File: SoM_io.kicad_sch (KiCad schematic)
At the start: 1 part, among them J2 Hermaphroditic_Molex_203456-0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

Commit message: [#81970] Refactor root
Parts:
- renumbered J2 to J1
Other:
- moved on the sheet: J1C, J1G, J1H, J1I, J1K

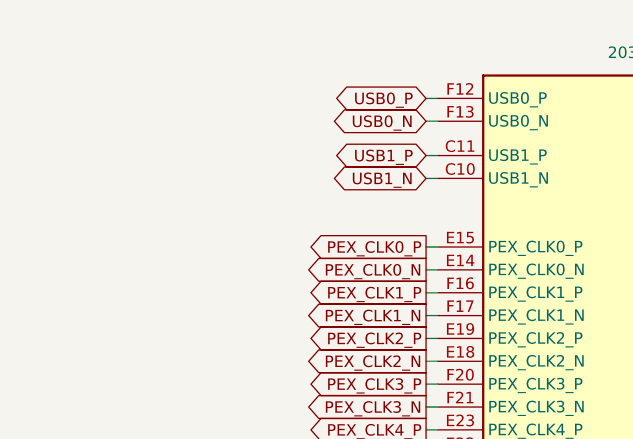
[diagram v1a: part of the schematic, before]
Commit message: [#82048] Add bus definitions and bus connections from M.2 key M to SoM
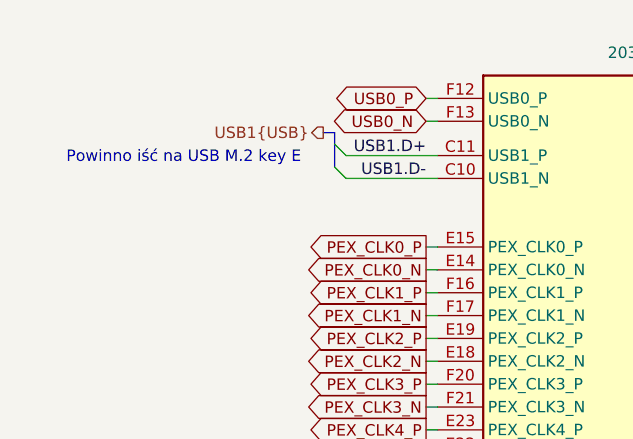
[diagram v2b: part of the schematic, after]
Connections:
- net USB1_N renamed USB1.D-
- net USB1_P renamed USB1.D+
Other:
- note added: "Powinno iść na USB M.2 key E"
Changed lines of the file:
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@@
 		(comment 1 "www.antmicro.com")
 	)
+	(text "Powinno iść na USB M.2 key E"
+		(exclude_from_sim no)
+		(at 89.916 68.834 0)
+		(effects
+			(font
+				(size 1.27 1.27)
+			)
+		)
+	)
+	(bus_entry
+		(at 107.95 68.58)
+		(size -1.27 -1.27)
+		(stroke
+			(width 0)
+			(type default)
+		)
+	)
+	(bus_entry
+		(at 107.95 71.12)
+		(size -1.27 -1.27)
+		(stroke
+			(width 0)
+			(type default)
+		)
+	)
 	(wire
 		(pts
@@
 		)
 	)
+	(bus
+		(pts
+			(xy 106.68 67.31) (xy 106.68 66.04)
+		)
+		(stroke
+			(width 0)
+			(type default)
+		)
+	)
 	(wire
 		(pts
@@
 	(wire
 		(pts
+			(xy 107.95 71.12) (xy 118.11 71.12)
+		)
+		(stroke
+			(width 0)
+			(type default)
+		)
+	)
+	(wire
+		(pts
 			(xy 166.37 165.1) (xy 163.83 165.1)
 		)
@@
 		)
 	)
+	(bus
+		(pts
+			(xy 106.68 66.04) (xy 105.41 66.04)
+		)
+		(stroke
+			(width 0)
+			(type default)
+		)
+	)
 	(wire
 		(pts
@@
 	(wire
 		(pts
-			(xy 116.84 71.12) (xy 118.11 71.12)
+			(xy 107.95 68.58) (xy 118.11 68.58)
 		)
 		(stroke
@@
 	(wire
 		(pts
-			(xy 116.84 68.58) (xy 118.11 68.58)
-		)
-		(stroke
-			(width 0)
-			(type default)
-		)
-	)
-	(wire
-		(pts
 			(xy 222.25 85.09) (xy 223.52 85.09)
 		)
@@
 		)
 	)
+	(bus
+		(pts
+			(xy 106.68 69.85) (xy 106.68 67.31)
+		)
+		(stroke
+			(width 0)
+			(type default)
+		)
+	)
 	(wire
 		(pts
@@
 		)
 	)
+	(label "USB1.D+"
+		(at 116.84 68.58 180)
+		(effects
+			(font
+				(size 1.27 1.27)
+			)
+			(justify right bottom)
+		)
+	)
+	(label "USB1.D-"
+		(at 116.84 71.12 180)
+		(effects
+			(font
+				(size 1.27 1.27)
+			)
+			(justify right bottom)
+		)
+	)
 	(global_label "GPIO08/DMIC3_5_DAT"
 		(shape input)
@@
 		)
 	)
-	(global_label "USB1_P"
-		(shape bidirectional)
-		(at 116.84 68.58 180)
-		(effects
-			(font
-				(size 1.27 1.27)
-			)
-			(justify right)
-		)
-		(property "Intersheetrefs" "${INTERSHEET_REFS}"
-			(at 116.84 68.58 0)
-			(effects
-				(font
-					(size 1.27 1.27)
-				)
-				(hide yes)
-			)
-		)
-	)
 	(global_label "PEX_C1_RST_N"
 		(shape output)
@@
 		)
 	)
-	(global_label "USB1_N"
-		(shape bidirectional)
-		(at 116.84 71.12 180)
-		(effects
-			(font
-				(size 1.27 1.27)
-			)
-			(justify right)
-		)
-		(property "Intersheetrefs" "${INTERSHEET_REFS}"
-			(at 116.84 71.12 0)
-			(effects
-				(font
-					(size 1.27 1.27)
-				)
-				(hide yes)
-			)
-		)
-	)
 	(global_label "UART1_TX"
 		(shape output)
@@
 		)
 	)
+	(hierarchical_label "USB1{USB}"
+		(shape output)
+		(at 105.41 66.04 180)
+		(effects
+			(font
+				(size 1.27 1.27)
+			)
+			(justify right)
+		)
+	)

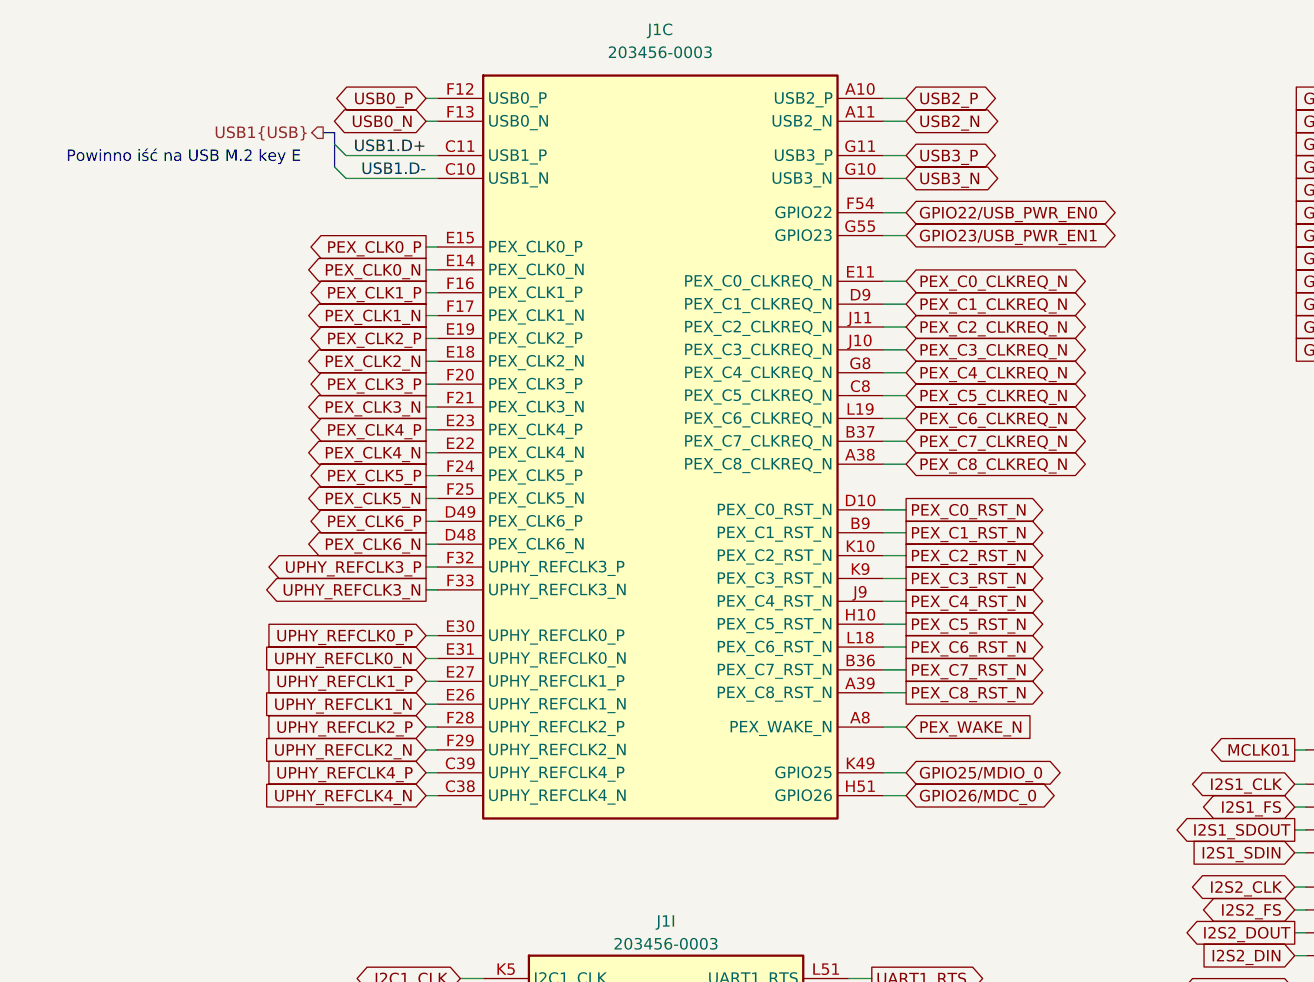
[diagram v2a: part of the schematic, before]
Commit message: [#82048] Continue routing bus connections from M.2 key M to SoM
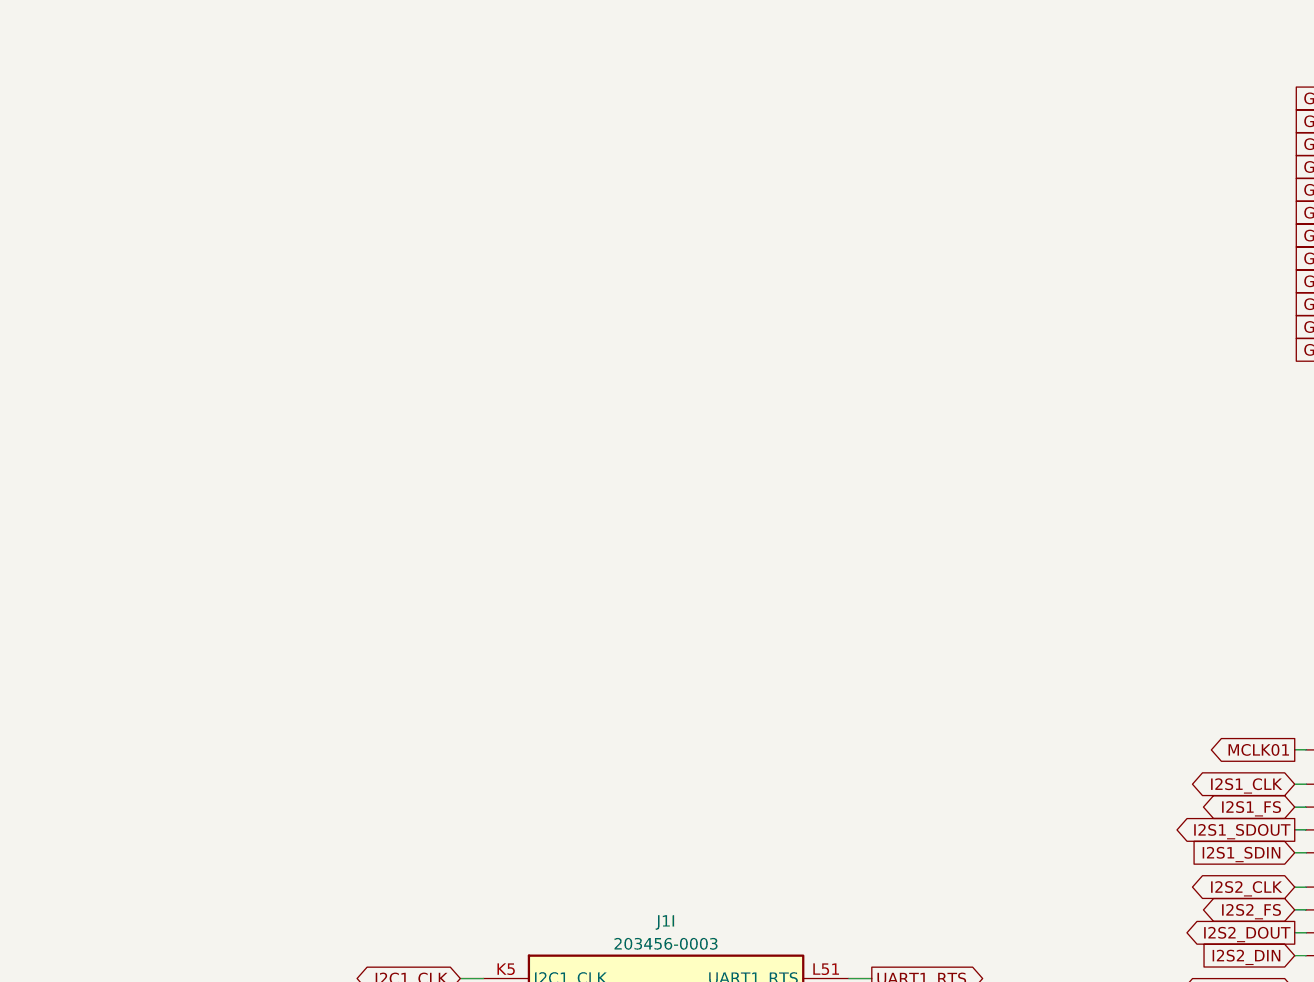
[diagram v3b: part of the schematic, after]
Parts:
- removed unit 3 of J1
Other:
- note removed: "Powinno iść na USB M.2 key E"

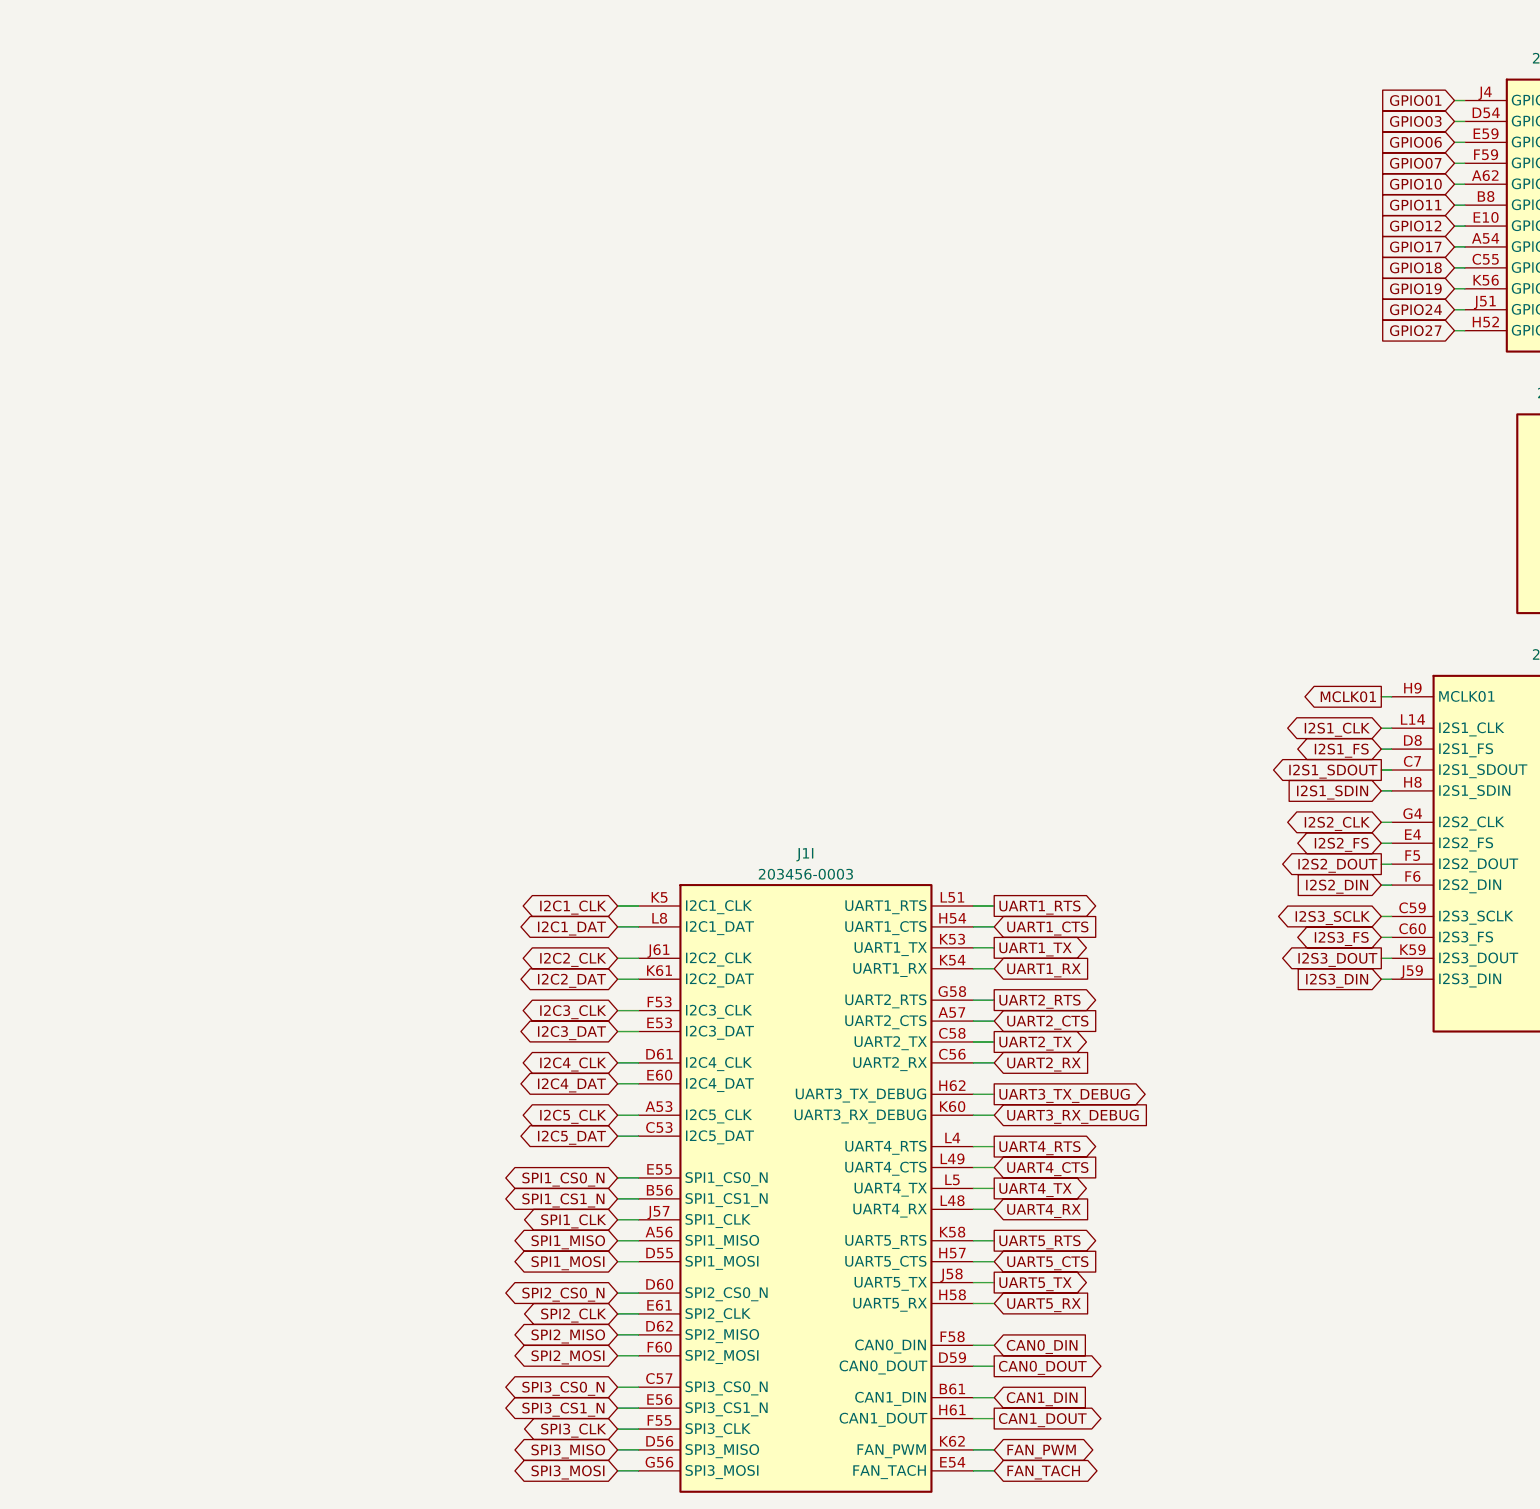
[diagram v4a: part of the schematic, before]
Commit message: [#82048] Route UART, I2S and I2C from M.2 key E to SoM
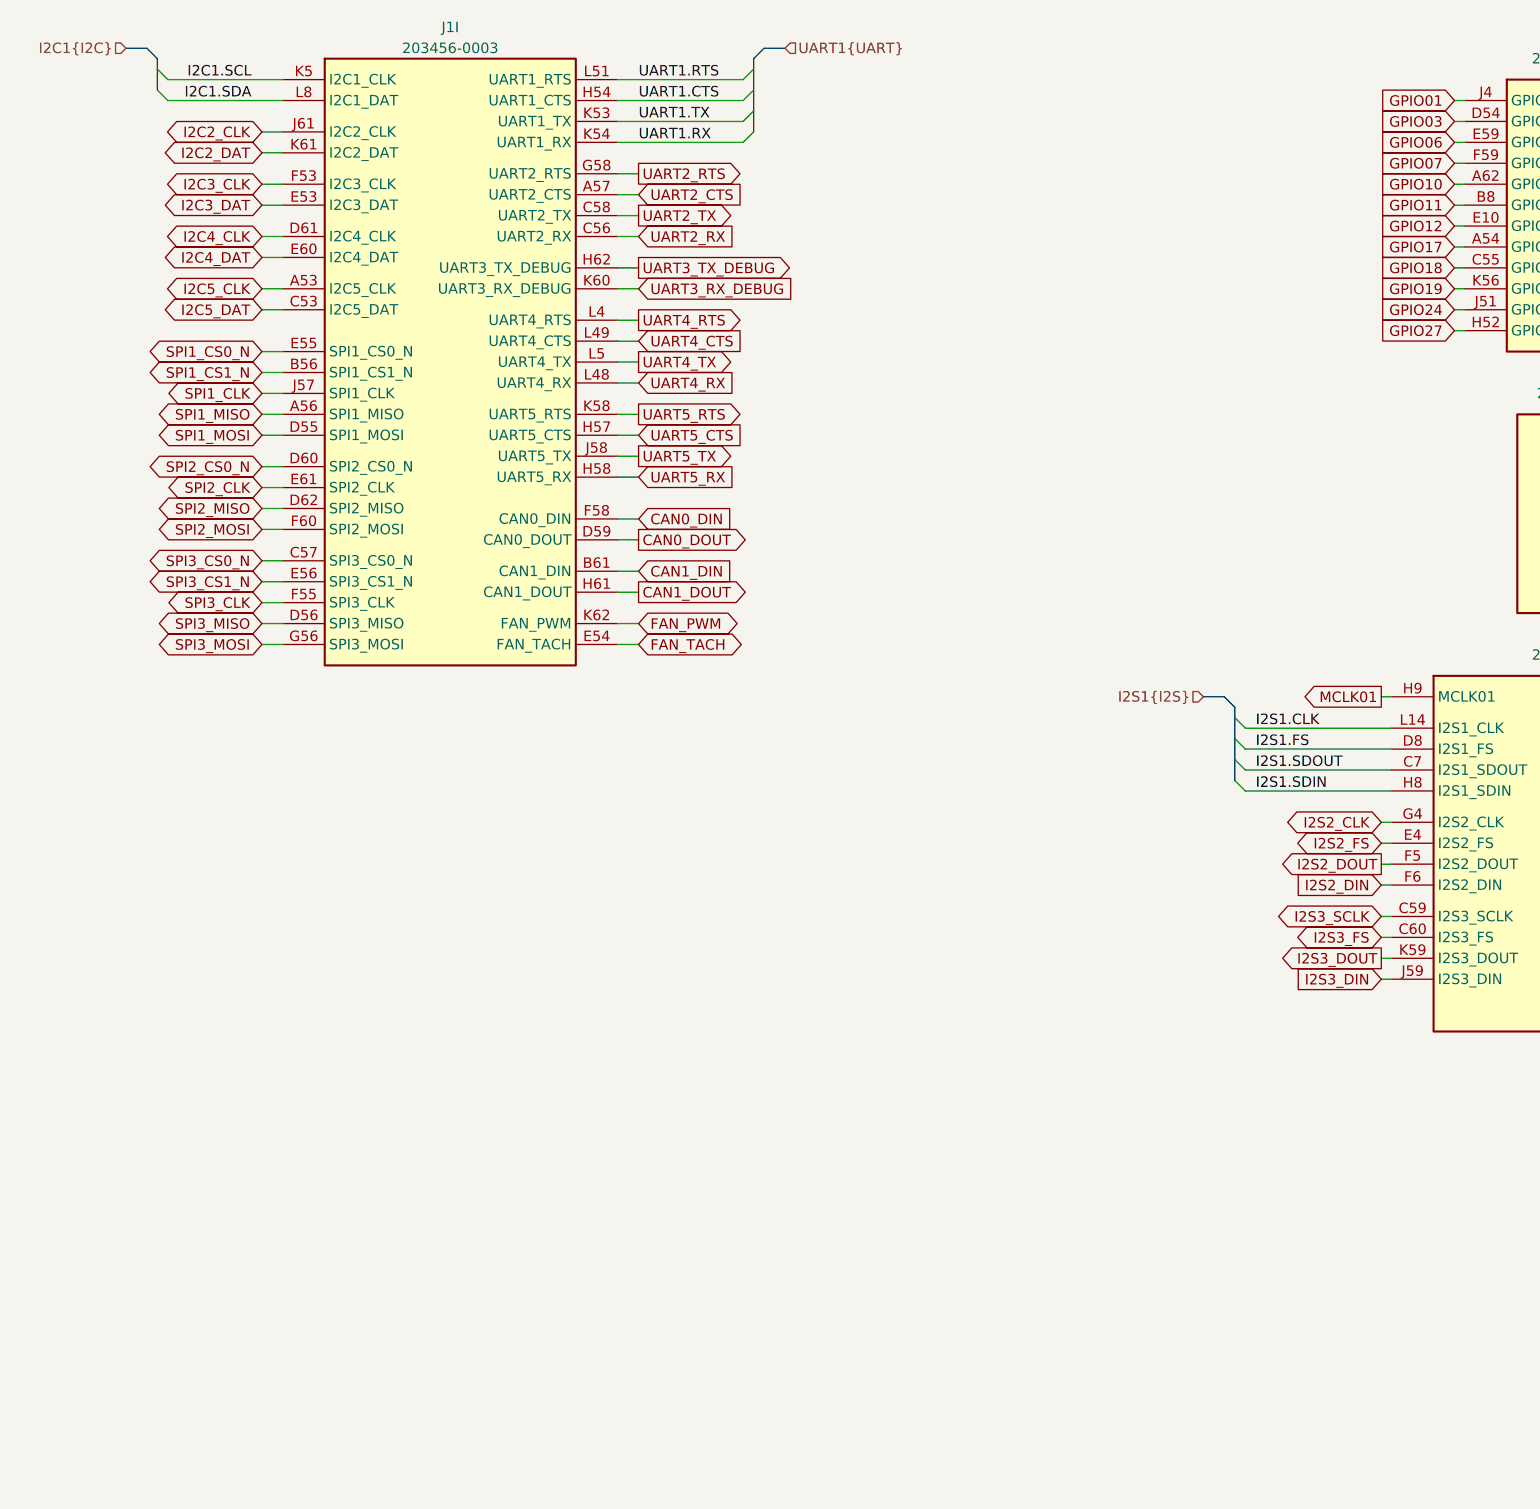
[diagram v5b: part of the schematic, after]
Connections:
- net I2C1_CLK renamed I2C1.SCL
- net I2C1_DAT renamed I2C1.SDA
- net I2S1_CLK renamed I2S1.CLK
- net I2S1_FS renamed I2S1.FS
- net I2S1_SDIN renamed I2S1.SDIN
- net I2S1_SDOUT renamed I2S1.SDOUT
- net UART1_CTS renamed UART1.CTS
- net UART1_RTS renamed UART1.RTS
- net UART1_RX renamed UART1.RX
- net UART1_TX renamed UART1.TX
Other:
- moved on the sheet: J1I

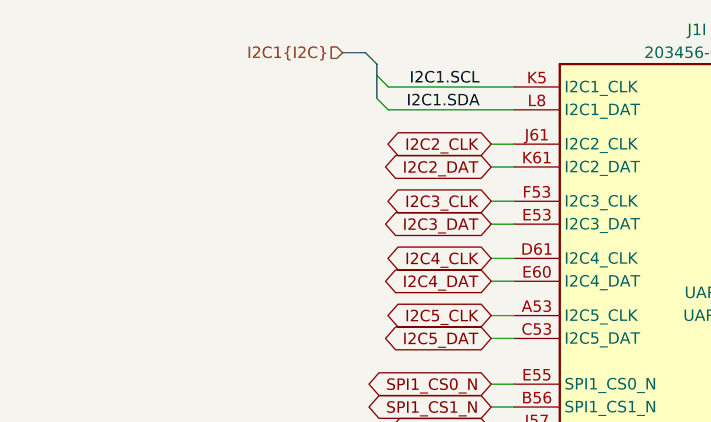
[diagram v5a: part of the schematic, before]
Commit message: [#81970] Connect SFI to SOM
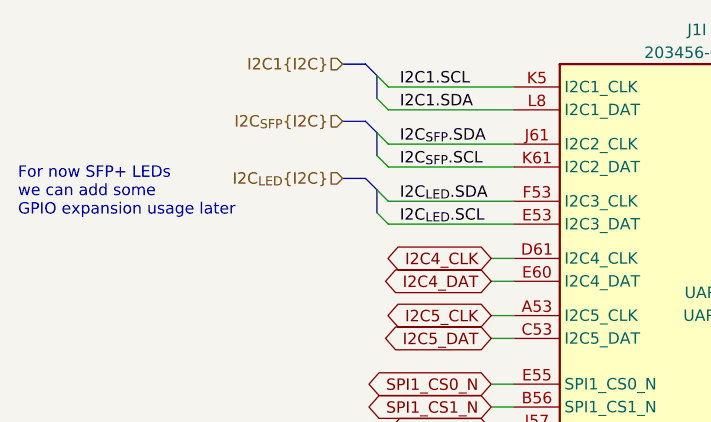
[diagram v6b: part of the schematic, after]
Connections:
- net I2C2_CLK renamed I2C_{SFP}.SDA
- net I2C2_DAT renamed I2C_{SFP}.SCL
- net I2C3_CLK renamed I2C_{LED}.SDA
- net I2C3_DAT renamed I2C_{LED}.SCL
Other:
- note added: "For now SFP+ LEDs we can add some GPIO expansion usage later"
